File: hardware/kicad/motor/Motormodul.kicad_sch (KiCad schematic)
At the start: 49 parts, among them J100 Stapelstecker 2x20, J101 Kettenstecker, Buchse oben (S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, J102 Kettenstecker, Stift unten (S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, J103 Leistungsstecker, Buchse oben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, J104 Leistungsstecker, Stift unten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, J3 Notaus-Ruhestrom, J5 Motor-Klemme, Q1 IRFR5305, U1 DRV8876PWPR, U100 STM32C011F6P6, U101 SN74LVC1G175, U102 SN74LVC2G00DCUR, U103 SN74LVC1G08, U3 SN74LVC1G08, U4 PC817, U5 PC817, U6 SN74LVC1G06, U7 SN74LVC1G06

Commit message: Aufgabe 5: Motormodul v2 (Notaus-Fix 1G06->1G07, Versorgungszelle statt Q1)
Notaus-Fix (Rot-Nachweis in TDD): U6/U7 liefen als SN74LVC1G06 (INVERTIERender
Open-Drain-NOT), waehrend saemtliche Doku/Pegelrechnung nichtinvertierendes
Verhalten voraussetzte -- das Board war fail-unsafe (intakte Schleife zog
Notaus, ein Drahtbruch gab ihn frei). Ersetzt durch SN74LVC1G07 (nicht-
invertierender OD-Puffer, pinidentisch, LCSC C7830). Datenblatt SCES296AG
per WebFetch selbst gelesen: Ii korrigiert (+-5uA statt +-1uA), kein
Schmitt-Trigger mehr (dokumentiert warum trotzdem sicher), Pin 1 (NC) ist
im 1G07-Symbol anders als im 1G06-Symbol ein echter Pin -> sch.nc() ergaenzt.

Q1/R11/R12/D1/C12 (falsch gepolter v1-Verpolschutz) entfernt, ersetzt durch
versorgung.bauen() (Task 3, Q90 richtig gepolt) + neuer Draht
_stapel_speist_lokal(), der PWR24V (Leistungsstecker) mit +24V (lokal,
hinter Q90) zusammenschliesst ("gespeiste Platine versorgt den Stapel").

Modul auf v2-Modulsockel umgestellt: einbauen(frei_durchreichen=True) +
randpads(sch) -- modulsockel.einbauen() bekam dafuer den neuen, rueckwaerts-
kompatiblen Parameter frei_durchreichen (Vorgabe False).

tests/test_motormodul.py: Notaus-Check woertlich aus dem Aufgabenbrief,
_BAUSTEINE/_LEITENDE_PAARE/_STECKER/_erwartet_*-Mengen auf v2 nachgezogen,
ERWARTETE_ERC_WARNUNGEN=3 (alle drei dokumentiert: lib_symbol_mismatch wie
in test_sockelplatine.py, isolated_pin_label fuer VSYS ohne Pico auf diesem
Modul, multiple_net_names fuer die absichtliche PWR24V/+24V-Verbindung).
tests/test_versorgung.py: alter ROT-NACHWEIS gegen Q1 durch POSITIV-Nachweis
gegen Q90 in der migrierten motormodul.py-Netzliste ersetzt.

ERC: 0 Fehler, 3 (dokumentierte) Warnungen. run_all.py-Rotliste:
test_erzeugte_dateien/test_sockelplatine/test_spec_dimmer/test_spec_motor/
test_spec_sockel -- alle nachweislich vorbestehend (sockelplatine.py-Bug
per git stash gegengeprueft), keins davon durch diese Aufgabe verursacht.

Bekannte Baustelle (nicht behoben, auss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
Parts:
- removed C12: 220u, Capacitor_THT:CP_Radial_D8.0mm_P3.50mm, symbol Device:C_Polarized
- removed D1: SMCJ30A, Diode_SMD:D_SMC_Handsoldering, symbol Device:D_Zener
- removed J100: Stapelstecker 2x20, Connector_PinHeader_2.54mm:PinHeader_2x20_P2.54mm_Vertical, symbol Connector_Generic:Conn_02x20_Odd_Even
- removed Q1: IRFR5305, Package_TO_SOT_SMD:TO-252-3_TabPin2, symbol Transistor_FET:Q_PMOS_GDS
- removed R11, R12: 10k, Resistor_SMD:R_0805_2012Metric_Pad1.20x1.40mm_HandSolder, symbol Device:R
- removed U6, U7: SN74LVC1G06, Package_TO_SOT_SMD:SOT-353_SC-70-5, symbol 74xGxx:74LVC1G06
- added C90: 220u, Capacitor_THT:CP_Radial_D8.0mm_P3.50mm, symbol Device:C_Polarized
- added C91: 22u, Capacitor_SMD:C_0805_2012Metric_Pad1.18x1.45mm_HandSolder, symbol Device:C
- added D90: SMCJ30A, Diode_SMD:D_SMC, symbol Device:D_Zener
- added D91: SS36C, Diode_SMD:D_SMC, symbol Device:D_Schottky
- added J100: Stapelstecker links, Pico-Pins 1..20 (Buchse), Connector_PinSocket_2.54mm:PinSocket_1x20_P2.54mm_Vertical, symbol Connector_Generic:Conn_01x20
- added J105: Stapelstecker rechts, Pico-Pins 21..40 (Buchse), Connector_PinSocket_2.54mm:PinSocket_1x20_P2.54mm_Vertical, symbol Connector_Generic:Conn_01x20
- added J90: Versorgung Eingang, TerminalBlock_Phoenix:TerminalBlock_Phoenix_PT-1,5-2-3.5-H_1x02_P3.50mm_Horizontal, symbol Connector:Screw_Terminal_01x02
- added J95: Randpads GPIO, unbestueckt (THT-Loetpad), Connector_PinHeader_2.54mm:PinHeader_1x18_P2.54mm_Vertical, symbol Connector_Generic:Conn_01x18
- added J96: Randpads Versorgung: 2x 3V3 + 2x GND, unbestueckt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, Connector_PinHeader_2.54mm:PinHeader_1x04_P2.54mm_Vertical, symbol Connector_Generic:Conn_01x04
- added Q90: IRFR5305, Package_TO_SOT_SMD:TO-252-3_TabPin2, symbol Transistor_FET:Q_PMOS_GDS
- added R90, R91: 10k, Resistor_SMD:R_0805_2012Metric_Pad1.20x1.40mm_HandSolder, symbol Device:R
- added U6, U7: SN74LVC1G07, Package_TO_SOT_SMD:SOT-353_SC-70-5, symbol 74xGxx:74LVC1G07
- added U90: K7805-1000R3, Converter_DCDC:Converter_DCDC_RECOM_R-78B-2.0_THT, symbol Converter_DCDC:R-78B5.0-2.0
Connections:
- net PWR24V is gone; now on net +24V: J103.1 (Pin_1), J103.3 (Pin_3), J104.1 (Pin_1), J104.3 (Pin_3)
- net +24V: now also C90.1, D90.1 (K), Q90.3 (S), R90.2, U90.1 (IN)
- net 3V3: now also C90.2, C91.2, D90.2 (A), J100.13 (Pin_13), J100.18 (Pin_18), J100.3 (Pin_3), J100.8 (Pin_8), J105.13 (Pin_13), J105.16 (Pin_16), J105.18 (Pin_18), J105.3 (Pin_3), J105.8 (Pin_8), J90.2 (Pin_2), J96.1 (Pin_1), J96.2 (Pin_2), J96.3 (Pin_3), J96.4 (Pin_4), R91.2, U6.3 (GND), U6.5 (VCC), U7.3 (GND), U7.5 (VCC), U90.2 (GND)
- net FLASH_MODE: now also J100.5 (Pin_5)
- net FLASH_RX: now also J100.2 (Pin_2)
- net FLASH_TX: now also J100.1 (Pin_1)
- net I2C_SCL: now also J100.7 (Pin_7)
- net I2C_SDA: now also J100.6 (Pin_6)
- net NOTAUS: now also J100.9 (Pin_9), U6.4, U7.4
- net SCHLEIFE_1: now also U6.2
- net SCHLEIFE_2: now also U7.2
- net SEL_CLK: now also J100.10 (Pin_10)
- new net +5V_LOKAL: C91.1, D91.2 (A), U90.3 (OUT)
- new net GP10: J100.14 (Pin_14), J95.3 (Pin_3)
- new net GP11: J100.15 (Pin_15), J95.4 (Pin_4)
- new net GP12: J100.16 (Pin_16), J95.5 (Pin_5)
- new net GP13: J100.17 (Pin_17), J95.6 (Pin_6)
- new net GP14: J100.19 (Pin_19), J95.7 (Pin_7)
- new net GP15: J100.20 (Pin_20), J95.8 (Pin_8)
- new net GP16: J105.1 (Pin_1), J95.9 (Pin_9)
- new net GP17: J105.2 (Pin_2), J95.10 (Pin_10)
- new net GP18: J105.4 (Pin_4), J95.11 (Pin_11)
- new net GP19: J105.5 (Pin_5), J95.12 (Pin_12)
- new net GP20: J105.6 (Pin_6), J95.13 (Pin_13)
- new net GP21: J105.7 (Pin_7), J95.14 (Pin_14)
- new net GP22: J105.9 (Pin_9), J95.15 (Pin_15)
- new net GP26: J105.11 (Pin_11), J95.16 (Pin_16)
- new net GP27: J105.12 (Pin_12), J95.17 (Pin_17)
- new net GP28: J105.14 (Pin_14), J95.18 (Pin_18)
- new net GP8: J100.11 (Pin_11), J95.1 (Pin_1)
- new net GP9: J100.12 (Pin_12), J95.2 (Pin_2)
- new net PWR_IN: J90.1 (Pin_1), Q90.2 (D)
- new net Q90_GATE: Q90.1 (G), R90.1, R91.1
- new net VSYS: D91.1 (K)
- no-connect marks 27 -> 11

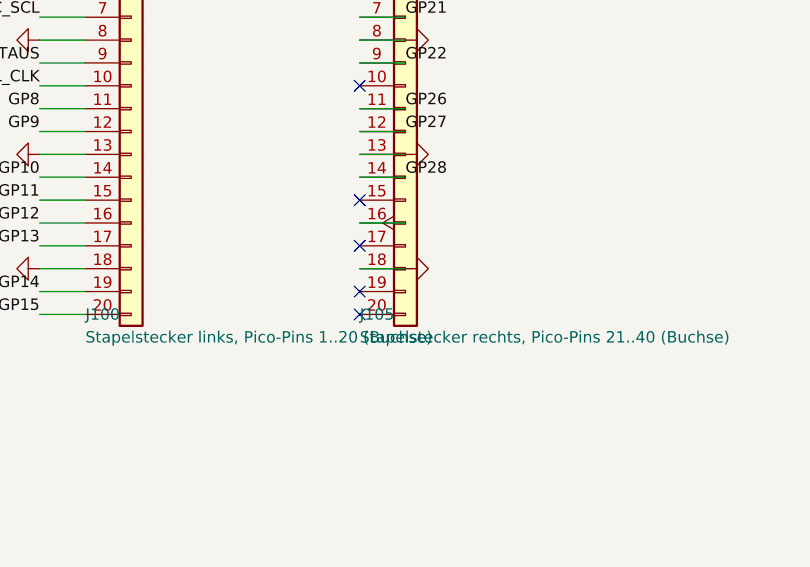
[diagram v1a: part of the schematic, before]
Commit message: Fix-Runde 1: VSYS (Pin 39) v2-belegbar -- Vertragswiderspruch behoben
Task-Review-Befund (tragend): stack_spec.NICHT_BELEGBAR verbot v1 jede
Einspeisung auf VSYS (Pin 39), weil niemand ihn trieb. Die v2-VERSORGUNG-
Zusage (vsys_diode=True) verlangt aber genau das Gegenteil -- jede
Versorgungszelle (versorgung.py, D91) speist VSYS ueber eine Schottky-
Diode. Der Vertrag verbot damit das Netz, das er selbst zusagt; D91s
Kathode landete auf einem Knoten ohne Verbraucher (isolated_pin_label-
ERC-Warnung im Motormodul).

TDD: tests/test_stack_spec.py zuerst um den Check
`IST_BELEGBAR(39) == True` ergaenzt (rot: False != True). Behoben in
tools/stack_spec.py -- Pin 39 aus NICHT_BELEGBAR entfernt, mit Herleitung
im Kommentar: die direkte, ungeschuetzte Verbindung bleibt verboten, nur
die Einspeisung UEBER die Entkopplungsdiode ist erlaubt (Zusatz-Satz bei
VERSORGUNG["vsys_diode"]). RUN/ADC_VREF/3V3_EN/VBUS unveraendert.

tools/sch/modulsockel.py: KEINE Verhaltensaenderung noetig -- eigene
Probe vor jeder Aenderung zeigte, dass _stapelstecker()s bestehender
else-Zweig Pin 39 automatisch auf "VSYS" verdrahtet, sobald IST_BELEGBAR
umschlaegt (STECKER_NETZE["VSYS"] existierte bereits). Nur ein
erklaerender Kommentar ergaenzt, keine Logik geaendert -- Abweichung vom
urspruenglichen Auftrag ("Pin verdrahten") dokumentiert, nicht verschwiegen.

Kollateral: modulsockel.py's eigener ERC-Testschritt bekommt dadurch eine
7. (statt 6.) isolated_pin_label-Warnung (VSYS jetzt verdrahtet, aber auf
dem nackten Sockelblatt ohne Gegenstueck) -- dieselbe Gattung wie die
bereits dokumentierten sechs, tests/test_modulsockel.py entsprechend
angepasst.

Motormodul neu erzeugt: ERC 0 Fehler / 2 Warnungen (lib_symbol_mismatch,
multiple_net_names) statt vorher 3 -- die VSYS-Warnung ist weg.
tests/test_motormodul.py: ERWARTETE_ERC_WARNUNGEN 3->2, zusaetzlich
(Review-Minor) das sortierte SET der Warnungstypen statt nur der Anzahl
geprueft, neuer Positivnachweis J105 Kontakt 19 -> D91.

Gruen: test_st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
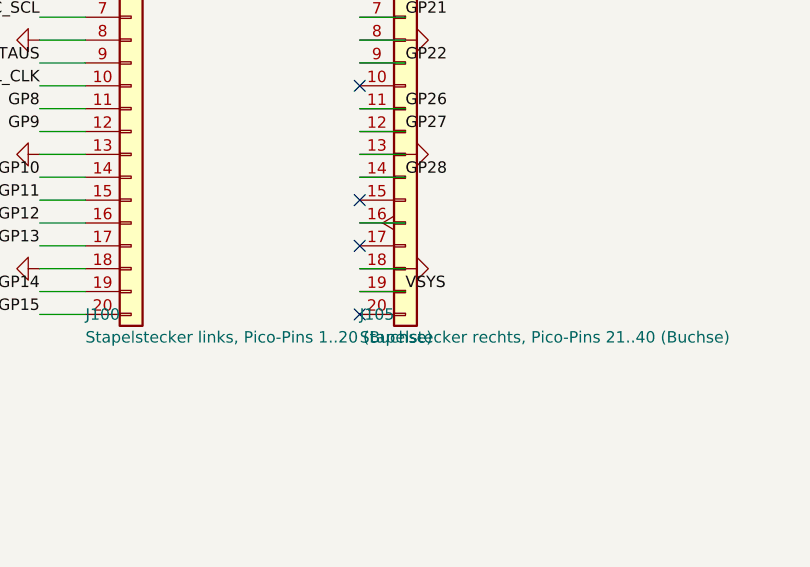
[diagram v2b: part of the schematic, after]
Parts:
- removed J100: Stapelstecker links, Pico-Pins 1..20 (Buchse), Connector_PinSocket_2.54mm:PinSocket_1x20_P2.54mm_Vertical, symbol Connector_Generic:Conn_01x20
- removed Q90: IRFR5305, Package_TO_SOT_SMD:TO-252-3_TabPin2, symbol Transistor_FET:Q_PMOS_GDS
- added C16: 0.1u, Capacitor_SMD:C_0805_2012Metric_Pad1.18x1.45mm_HandSolder, symbol Device:C
- added J96: Randpads Versorgung: 2x 3V3 + 2x GND, unbestueckt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, Connector_PinHeader_2.54mm:PinHeader_1x04_P2.54mm_Vertical, symbol Connector_Generic:Conn_01x04
- C10: renamed from C11; value 0.1u -> 0.022u
- C100: renamed from U101; value SN74LVC1G175 -> 100n; footprint Package_TO_SOT_SMD:SOT-363_SC-70-6 -> Capacitor_SMD:C_0805_2012Metric_Pad1.18x1.45mm_HandSolder; symbol 74xGxx:74LVC1G175 -> Device:C
- C101: renamed from U102; value SN74LVC2G00DCUR -> 1000n; footprint Package_SO:VSSOP-8_2.3x2mm_P0.5mm -> Capacitor_SMD:C_0805_2012Metric_Pad1.18x1.45mm_HandSolder; symbol 74xGxx:74LVC2G00 -> Device:C
- C11: renamed from R7; value 0.1k -> 0.1u; footprint Resistor_SMD:R_0805_2012Metric_Pad1.20x1.40mm_HandSolder -> Capacitor_SMD:C_0805_2012Metric_Pad1.18x1.45mm_HandSolder; symbol Device:R -> Device:C
- C13: renamed from J5; value Motor-Klemme -> 0.1u; footprint TerminalBlock_Phoenix:TerminalBlock_Phoenix_MKDS-3-2-5.08_1x02_P5.08mm_Horizontal -> Capacitor_SMD:C_0805_2012Metric_Pad1.18x1.45mm_HandSolder; symbol Connector:Screw_Terminal_01x02 -> Device:C
- C14: renamed from R15; value 10k -> 0.1u; footprint Resistor_SMD:R_0805_2012Metric_Pad1.20x1.40mm_HandSolder -> Capacitor_SMD:C_0805_2012Metric_Pad1.18x1.45mm_HandSolder; symbol Device:R -> Device:C
- C15: renamed from R17; value 3.3k -> 0.1u; footprint Resistor_SMD:R_1206_3216Metric -> Capacitor_SMD:C_0805_2012Metric_Pad1.18x1.45mm_HandSolder; symbol Device:R -> Device:C
- C9: renamed from C10; value 0.022u -> 0.1u
- C90: renamed from U90; value K7805-1000R3 -> 220u; footprint Converter_DCDC:Converter_DCDC_RECOM_R-78B-2.0_THT -> Capacitor_THT:CP_Radial_D8.0mm_P3.50mm; symbol Converter_DCDC:R-78B5.0-2.0 -> Device:C_Polarized
- C91: renamed from D91; value SS36C -> 22u; footprint Diode_SMD:D_SMC -> Capacitor_SMD:C_0805_2012Metric_Pad1.18x1.45mm_HandSolder; symbol Device:D_Schottky -> Device:C
- D90: renamed from C90; value 220u -> SMCJ30A; footprint Capacitor_THT:CP_Radial_D8.0mm_P3.50mm -> Diode_SMD:D_SMC; symbol Device:C_Polarized -> Device:D_Zener
- D91: renamed from U1; value DRV8876PWPR -> SS36C; footprint DRV8876PWPR:IC_DRV8876PWPR -> Diode_SMD:D_SMC; symbol DRV8876PWPR:DRV8876PWPR -> Device:D_Schottky
- J100: renamed from J105; value Stapelstecker rechts, Pico-Pins 21..40 (Buchse) -> Stapelstecker links, Pico-Pins 1..20 (Buchse)
- J101: renamed from J102; value Kettenstecker, Stift unten (SMD) -> Kettenstecker, Buchse oben (SMD); footprint Connector_PinHeader_2.54mm:PinHeader_1x02_P2.54mm_Vertical_SMD_Pin1Left -> Connector_PinSocket_2.54mm:PinSocket_1x02_P2.54mm_Vertical_SMD_Pin1Left
- J102: renamed from J103; value Leistungsstecker, Buchse oben (SMD) -> Kettenstecker, Stift unten (SMD); footprint Connector_PinSocket_2.54mm:PinSocket_2x02_P2.54mm_Vertical_SMD -> Connector_PinHeader_2.54mm:PinHeader_1x02_P2.54mm_Vertical_SMD_Pin1Left; symbol Connector_Generic:Conn_02x02_Odd_Even -> Connector_Generic:Conn_01x02
- J103: renamed from J104; value Leistungsstecker, Stift unten (SMD) -> Leistungsstecker, Buchse oben (SMD); footprint Connector_PinHeader_2.54mm:PinHeader_2x02_P2.54mm_Vertical_SMD -> Connector_PinSocket_2.54mm:PinSocket_2x02_P2.54mm_Vertical_SMD
- J104: renamed from U100; value STM32C011F6P6 -> Leistungsstecker, Stift unten (SMD); footprint Package_SO:TSSOP-20_4.4x6.5mm_P0.65mm -> Connector_PinHeader_2.54mm:PinHeader_2x02_P2.54mm_Vertical_SMD; symbol MCU_ST_STM32C0:STM32C011F6Px -> Connector_Generic:Conn_02x02_Odd_Even
- J105: renamed from J101; value Kettenstecker, Buchse oben (SMD) -> Stapelstecker rechts, Pico-Pins 21..40 (Buchse); footprint Connector_PinSocket_2.54mm:PinSocket_1x02_P2.54mm_Vertical_SMD_Pin1Left -> Connector_PinSocket_2.54mm:PinSocket_1x20_P2.54mm_Vertical; symbol Connector_Generic:Conn_01x02 -> Connector_Generic:Conn_01x20
- J3: renamed from R16; value 3.3k -> Notaus-Ruhestrom; footprint Resistor_SMD:R_1206_3216Metric -> Connector_PinHeader_2.54mm:PinHeader_1x04_P2.54mm_Vertical; symbol Device:R -> Connector:Conn_01x04_Pin
- J5: renamed from U3; value SN74LVC1G08 -> Motor-Klemme; footprint Package_TO_SOT_SMD:SOT-353_SC-70-5 -> TerminalBlock_Phoenix:TerminalBlock_Phoenix_MKDS-3-2-5.08_1x02_P5.08mm_Horizontal; symbol 74xGxx:74LVC1G08 -> Connector:Screw_Terminal_01x02
- J95: renamed from J96; value Randpads Versorgung: 2x 3V3 + 2x GND, unbestueckt (THT-Loetpad) -> Randpads GPIO, unbestueckt (THT-Loetpad); footprint Connector_PinHeader_2.54mm:PinHeader_1x04_P2.54mm_Vertical -> Connector_PinHeader_2.54mm:PinHeader_1x18_P2.54mm_Vertical; symbol Connector_Generic:Conn_01x04 -> Connector_Generic:Conn_01x18
- Q90: renamed from R90; value 10k -> IRFR5305; footprint Resistor_SMD:R_0805_2012Metric_Pad1.20x1.40mm_HandSolder -> Package_TO_SOT_SMD:TO-252-3_TabPin2; symbol Device:R -> Transistor_FET:Q_PMOS_GDS
- R10: renamed from C13; value 0.1u -> 4.7k; footprint Capacitor_SMD:C_0805_2012Metric_Pad1.18x1.45mm_HandSolder -> Resistor_SMD:R_0805_2012Metric_Pad1.20x1.40mm_HandSolder; symbol Device:C -> Device:R; now not fitted
- R100: renamed from R105; value 10000 (ID_OBEN) -> Kennwiderstand (Modultyp)
- R101: renamed from J95; value Randpads GPIO, unbestueckt (THT-Loetpad) -> Kennwiderstand (Modultyp); footprint Connector_PinHeader_2.54mm:PinHeader_1x18_P2.54mm_Vertical -> Resistor_SMD:R_0805_2012Metric_Pad1.20x1.40mm_HandSolder; symbol Connector_Generic:Conn_01x18 -> Device:R; now fitted
- R102: renamed from C101; value 1000n -> 100k; footprint Capacitor_SMD:C_0805_2012Metric_Pad1.18x1.45mm_HandSolder -> Resistor_SMD:R_0805_2012Metric_Pad1.20x1.40mm_HandSolder; symbol Device:C -> Device:R
- R104: renamed from R100; value Kennwiderstand (Modultyp) -> 10000 (ID_OBEN)
- R105: renamed from R101; value Kennwiderstand (Modultyp) -> 10000 (ID_OBEN)
- R13: renamed from R5; value 1.3k -> 10k
- R15: renamed from J3; value Notaus-Ruhestrom -> 10k; footprint Connector_PinHeader_2.54mm:PinHeader_1x04_P2.54mm_Vertical -> Resistor_SMD:R_0805_2012Metric_Pad1.20x1.40mm_HandSolder; symbol Connector:Conn_01x04_Pin -> Device:R
- R18: renamed from U4; value PC817 -> 3.3k; footprint Optocoupler_PC817:PC817_SMT_Gullwing -> Resistor_SMD:R_1206_3216Metric; symbol Isolator:PC817 -> Device:R
- R19: renamed from U5; value PC817 -> 3.3k; footprint Optocoupler_PC817:PC817_SMT_Gullwing -> Resistor_SMD:R_1206_3216Metric; symbol Isolator:PC817 -> Device:R
- R20: renamed from U6; value SN74LVC1G07 -> 4.7k; footprint Package_TO_SOT_SMD:SOT-353_SC-70-5 -> Resistor_SMD:R_0805_2012Metric_Pad1.20x1.40mm_HandSolder; symbol 74xGxx:74LVC1G07 -> Device:R; LCSC C7830 -> (none)
- R21: renamed from U7; value SN74LVC1G07 -> 4.7k; footprint Package_TO_SOT_SMD:SOT-353_SC-70-5 -> Resistor_SMD:R_0805_2012Metric_Pad1.20x1.40mm_HandSolder; symbol 74xGxx:74LVC1G07 -> Device:R; LCSC C7830 -> (none)
- R5: renamed from R10; value 4.7k -> 1.3k; now fitted
- R9: renamed from R13; value 10k -> 0.1k
- R91: renamed from D90; value SMCJ30A -> 10k; footprint Diode_SMD:D_SMC -> Resistor_SMD:R_0805_2012Metric_Pad1.20x1.40mm_HandSolder; symbol Device:D_Zener -> Device:R
- U1: renamed from C9; value 0.1u -> DRV8876PWPR; footprint Capacitor_SMD:C_0805_2012Metric_Pad1.18x1.45mm_HandSolder -> DRV8876PWPR:IC_DRV8876PWPR; symbol Device:C -> DRV8876PWPR:DRV8876PWPR
- U100: renamed from C100; value 100n -> STM32C011F6P6; footprint Capacitor_SMD:C_0805_2012Metric_Pad1.18x1.45mm_HandSolder -> Package_SO:TSSOP-20_4.4x6.5mm_P0.65mm; symbol Device:C -> MCU_ST_STM32C0:STM32C011F6Px
- U101: renamed from R102; value 100k -> SN74LVC1G175; footprint Resistor_SMD:R_0805_2012Metric_Pad1.20x1.40mm_HandSolder -> Package_TO_SOT_SMD:SOT-363_SC-70-6; symbol Device:R -> 74xGxx:74LVC1G175
- U102: renamed from U103; value SN74LVC1G08 -> SN74LVC2G00DCUR; footprint Package_TO_SOT_SMD:SOT-353_SC-70-5 -> Package_SO:VSSOP-8_2.3x2mm_P0.5mm; symbol 74xGxx:74LVC1G08 -> 74xGxx:74LVC2G00
- U103: renamed from R104; value 10000 (ID_OBEN) -> SN74LVC1G08; footprint Resistor_SMD:R_0805_2012Metric_Pad1.20x1.40mm_HandSolder -> Package_TO_SOT_SMD:SOT-353_SC-70-5; symbol Device:R -> 74xGxx:74LVC1G08
- U3: renamed from C14; value 0.1u -> SN74LVC1G08; footprint Capacitor_SMD:C_0805_2012Metric_Pad1.18x1.45mm_HandSolder -> Package_TO_SOT_SMD:SOT-353_SC-70-5; symbol Device:C -> 74xGxx:74LVC1G08
- U4: renamed from R20; value 4.7k -> PC817; footprint Resistor_SMD:R_0805_2012Metric_Pad1.20x1.40mm_HandSolder -> Optocoupler_PC817:PC817_SMT_Gullwing; symbol Device:R -> Isolator:PC817
- U5: renamed from R21; value 4.7k -> PC817; footprint Resistor_SMD:R_0805_2012Metric_Pad1.20x1.40mm_HandSolder -> Optocoupler_PC817:PC817_SMT_Gullwing; symbol Device:R -> Isolator:PC817
- U6: renamed from C15; value 0.1u -> SN74LVC1G07; footprint Capacitor_SMD:C_0805_2012Metric_Pad1.18x1.45mm_HandSolder -> Package_TO_SOT_SMD:SOT-353_SC-70-5; symbol Device:C -> 74xGxx:74LVC1G07; LCSC (none) -> C7830
- U7: renamed from C16; value 0.1u -> SN74LVC1G07; footprint Capacitor_SMD:C_0805_2012Metric_Pad1.18x1.45mm_HandSolder -> Package_TO_SOT_SMD:SOT-353_SC-70-5; symbol Device:C -> 74xGxx:74LVC1G07; LCSC (none) -> C7830
- U90: renamed from C91; value 22u -> K7805-1000R3; footprint Capacitor_SMD:C_0805_2012Metric_Pad1.18x1.45mm_HandSolder -> Converter_DCDC:Converter_DCDC_RECOM_R-78B-2.0_THT; symbol Device:C -> Converter_DCDC:R-78B5.0-2.0
- renumbered R18 to R16, R19 to R17, R8 to R7, R9 to R8, R91 to R90
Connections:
- net +24V: now also C11.2, C9.1, J104.1 (Pin_1), J104.3 (Pin_3), Q90.3 (S), R16.1, R17.1, R90.2, U1.11 (VM), U90.1 (IN); no longer C10.2, C15.1, D91.11 (VM), J102.1 (Pin_1), J102.3 (Pin_3), J3.1, Q90.2, R91.1 (K), U1.1
- net +5V_LOKAL: now also C91.1, D91.2 (A), U90.3 (OUT); no longer C90.3 (OUT), C91.2 (A), U90.1
- net 3V3: now also C100.1, C101.2, C11.1, C13.2, C14.2, C15.1, C15.2, C91.2, J104.2 (Pin_2), J105.13 (Pin_13), J105.16 (Pin_16), J105.18 (Pin_18), J105.3 (Pin_3), J105.8 (Pin_8), R100.2, R101.2, R102.1, R104.1, R105.1, R13.1, R15.1, R20.2, R21.2, U1.15 (GND), U1.16 (PMODE), U1.17 (EXP), U1.5 (VREF), U1.7 (IMODE), U1.9 (PGND), U100.4 (VDD), U100.5 (VSS), U101.2 (GND), U101.5 (VCC), U102.4 (GND), U102.8 (VCC), U103.3 (GND), U103.5 (VCC), U3.3 (GND), U3.5 (VCC), U4.4, U5.4, U6.3 (GND), U6.5 (VCC), U7.3 (GND), U7.5 (VCC), C16.1, C16.2, J96.1 (Pin_1), J96.2 (Pin_2), J96.3 (Pin_3), J96.4 (Pin_4); no longer C10.1, C100.5 (VCC), D91.15 (GND), D91.16 (PMODE), D91.17 (EXP), D91.5 (VREF), D91.7 (IMODE), D91.9 (PGND), J100.16 (Pin_16), J102.4 (Pin_4), J104.5 (VSS), J105.2 (Pin_2), J5.3 (GND), J5.5 (VCC), J95.1 (Pin_1), J95.2 (Pin_2), J95.3 (Pin_3), J95.4 (Pin_4), R100.1, R102.2, R104.2, R105.2, R13.2, R18.2, R18.4, R19.2, R19.4, R20.3 (GND), R20.5 (VCC), R21.3 (GND), R21.5 (VCC), R9.1, R90.2, U100.1, U100.2, U101.1, U102.3 (GND), U102.4 (GND), U102.5 (VCC), U102.8 (VCC), U103.1, U3.1, U3.2, U6.1, U6.2, U7.1, U7.2
- net BOOT0: now also U100.19 (PA14), U103.4; no longer J104.19 (PA14), U102.4
- net CPH: now also C10.1, U1.13 (CPH); no longer C9.1, D91.13 (CPH)
- net CPL: now also C10.2, U1.14 (CPL); no longer C9.2, D91.14 (CPL)
- net FLASH_MODE: now also J100.5 (Pin_5), U102.5, U103.1; no longer U102.1, U102.5
- net FLASH_RX: now also J100.2 (Pin_2), U100.16 (PA9/PA11); no longer J104.16 (PA9/PA11)
- net FLASH_TX: now also J100.1 (Pin_1), U100.17 (PA10/PA12); no longer J104.17 (PA10/PA12)
- net GP10: now also J100.14 (Pin_14), J95.3 (Pin_3); no longer R101.3 (Pin_3)
- net GP11: now also J100.15 (Pin_15), J95.4 (Pin_4); no longer R101.4 (Pin_4)
- net GP12: now also J100.16 (Pin_16), J95.5 (Pin_5); no longer R101.5 (Pin_5)
- net GP13: now also J100.17 (Pin_17), J95.6 (Pin_6); no longer R101.6 (Pin_6)
- net GP14: now also J100.19 (Pin_19), J95.7 (Pin_7); no longer R101.7 (Pin_7)
- net GP15: now also J100.20 (Pin_20), J95.8 (Pin_8); no longer R101.8 (Pin_8)
- net GP16: now also J105.1 (Pin_1), J95.9 (Pin_9); no longer J100.1 (Pin_1), R101.9 (Pin_9)
- net GP17: now also J105.2 (Pin_2), J95.10 (Pin_10); no longer J100.2 (Pin_2), R101.10 (Pin_10)
- net GP18: now also J105.4 (Pin_4), J95.11 (Pin_11); no longer J100.4 (Pin_4), R101.11 (Pin_11)
- net GP19: now also J105.5 (Pin_5), J95.12 (Pin_12); no longer J100.5 (Pin_5), R101.12 (Pin_12)
- net GP20: now also J105.6 (Pin_6), J95.13 (Pin_13); no longer J100.6 (Pin_6), R101.13 (Pin_13)
- net GP21: now also J105.7 (Pin_7), J95.14 (Pin_14); no longer J100.7 (Pin_7), R101.14 (Pin_14)
- net GP22: now also J105.9 (Pin_9), J95.15 (Pin_15); no longer J100.9 (Pin_9), R101.15 (Pin_15)
- net GP26: now also J105.11 (Pin_11), J95.16 (Pin_16); no longer J100.11 (Pin_11), R101.16 (Pin_16)
- net GP27: now also J105.12 (Pin_12), J95.17 (Pin_17); no longer J100.12 (Pin_12), R101.17 (Pin_17)
- net GP28: now also J105.14 (Pin_14), J95.18 (Pin_18); no longer J100.14 (Pin_14), R101.18 (Pin_18)
- net GP8: now also J100.11 (Pin_11), J95.1 (Pin_1); no longer R101.1 (Pin_1)
- net GP9: now also J100.12 (Pin_12), J95.2 (Pin_2); no longer R101.2 (Pin_2)
- net I2C_SCL: now also J100.7 (Pin_7), U100.20 (PB6); no longer J104.20 (PB6)
- net I2C_SDA: now also J100.6 (Pin_6), U100.1 (PB7); no longer J104.1 (PB7)
- net ID0: now also R100.1, R104.2, U100.7 (PA0); no longer J104.7 (PA0), R104.1, U103.2
- net ID1: now also R101.1, R105.2, U100.8 (PA1); no longer J104.8 (PA1), R100.2, R105.1
- net IN1: now also R7.1, U100.9 (PA2); no longer C11.1, J104.9 (PA2)
- net IN2: now also R8.1, U100.10 (PA3); no longer J104.10 (PA3), R7.1
- net IPROPI: now also C13.1, U1.6 (IPROPI), U100.13 (PA6); no longer D91.6 (IPROPI), J104.13 (PA6), R13.1
- net KREIS1_A: now also J3.1 (Pin_1), R16.2; no longer J3.2, R15.1 (Pin_1)
- net KREIS1_B: now also J3.2 (Pin_2), R18.1; no longer R15.2 (Pin_2), R16.1
- net KREIS2_A: now also J3.3 (Pin_3), R17.2; no longer C15.2, R15.3 (Pin_3)
- net KREIS2_B: now also J3.4 (Pin_4), R19.1; no longer R15.4 (Pin_4), R17.1
- net NCLR: now also C101.1, R102.2, U101.6 (~{CLR}); no longer C100.6 (~{CLR}), R102.1, U101.2
- net NFAULT: now also R13.2, U1.4 (~{NFAULT}), U100.12 (PA5); no longer D91.4 (~{NFAULT}), J104.12 (PA5), R9.2
- net NOTAUS: now also J100.9 (Pin_9), R15.2, U3.2, U6.4, U7.4; no longer C14.2, J5.2, R20.4, R21.4
- net NQ: now also U102.6, U102.7; no longer C101.7, U102.6
- net NRST: now also U100.6 (PF2), U102.3; no longer J104.6 (PF2), U102.3
- net NSLEEP: now also R9.1, U100.11 (PA4); no longer J104.11 (PA4), R8.1
- net NSLEEP_GATTER: now also R9.2, U3.1; no longer J5.1, R8.2
- net Out1: now also J5.1 (Pin_1), U1.8 (OUT1); no longer C13.1 (Pin_1), D91.8 (OUT1)
- net Out2: now also J5.2 (Pin_2), U1.10 (OUT2); no longer C13.2 (Pin_2), D91.10 (OUT2)
- net PWR_IN: now also Q90.2 (D)
- net Q90_GATE: now also R91.1
- net SCHLEIFE_1: now also R20.1, U100.3 (PC15), U4.3, U6.2; no longer J104.3 (PC15), R18.3, R20.2, U4.1
- net SCHLEIFE_2: now also R21.1, U100.14 (PA7), U5.3, U7.2; no longer J104.14 (PA7), R19.3, R21.2, U5.1
- net SEL_CLK: now also J100.10 (Pin_10), U101.1 (C); no longer C100.1 (C)
- net SEL_IN: now also J101.1 (Pin_1), U101.3 (D); no longer C100.3 (D), J105.1 (Pin_1)
- net SEL_OUT: now also J102.1 (Pin_1), U101.4 (Q), U102.1, U102.2, U103.2; no longer C100.4 (Q), C101.1, C101.2, J101.1 (Pin_1), U102.2
- net U1_EN_IN1: now also R7.2, U1.1 (EN/IN1); no longer C11.2, D91.1 (EN/IN1)
- net U1_NSLEEP: now also U1.3 (NSLEEP), U3.4; no longer D91.3 (NSLEEP), J5.4
- net U1_PH_IN2: now also R8.2, U1.2 (PH/IN2); no longer D91.2 (PH/IN2), R7.2
- net U4_LED_A: now also R18.2, U4.1; no longer R16.2, R18.1
- net U5_LED_A: now also R19.2, U5.1; no longer R17.2, R19.1
- net VCP: now also C9.2, U1.12 (VCP); no longer D91.12 (VCP), U1.2
- net VSYS: now also D91.1 (K), J105.19 (Pin_19); no longer C91.1 (K)
- no-connect marks 11 -> 10
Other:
- moved on the sheet: C10, C9, J100, J101, J103, R100, R104, R105, R13, R16, R17, R7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
